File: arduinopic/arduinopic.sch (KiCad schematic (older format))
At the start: 19 parts, among them Q1 BC847, U1 PIC16F628-xxIP, U2 PIC16F610-IP

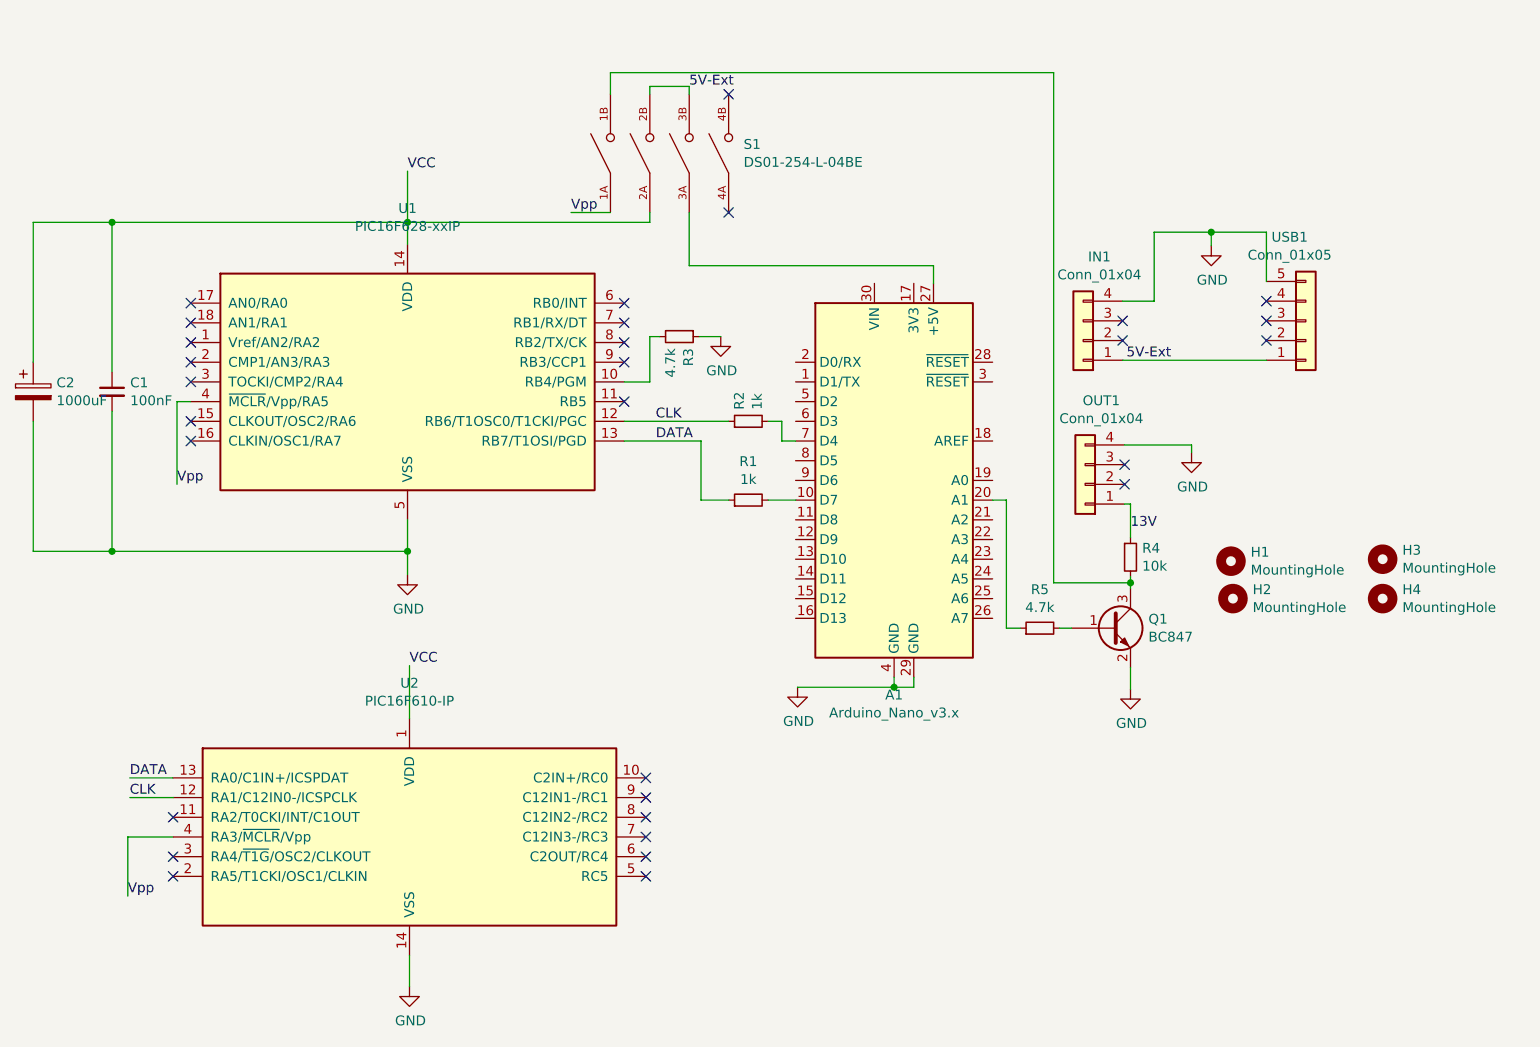
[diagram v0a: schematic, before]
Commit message: PIC12F629, PIC12F675 support added
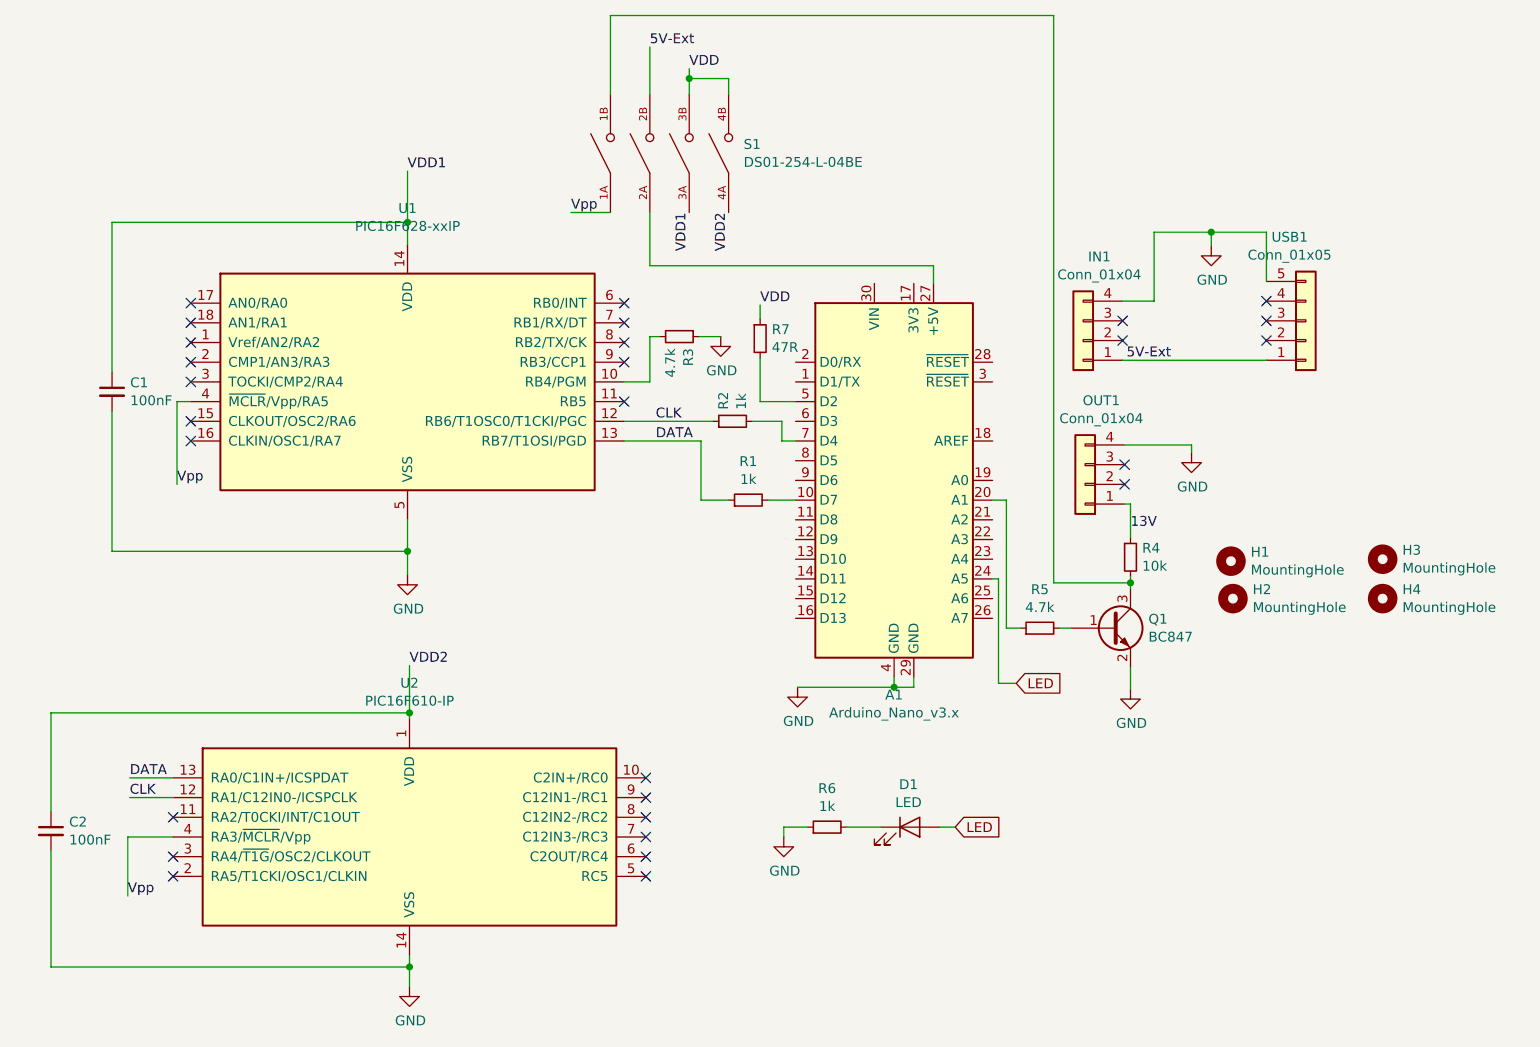
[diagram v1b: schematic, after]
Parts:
- removed C2: 1000uF, Capacitor_THT:CP_Radial_D10.0mm_P5.00mm, symbol Device:CP
- added C2: 100nF, Capacitor_SMD:C_1206_3216Metric_Pad1.42x1.75mm_HandSolder, symbol Device:C_Small
- added D1: LED, LED_SMD:LED_1206_3216Metric_Pad1.42x1.75mm_HandSolder, symbol Device:LED
- added R6: 1k, Resistor_SMD:R_1206_3216Metric_Pad1.42x1.75mm_HandSolder, symbol Device:R_Small
- added R7: 47R, Resistor_SMD:R_1206_3216Metric_Pad1.42x1.75mm_HandSolder, symbol Device:R_Small
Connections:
- net 5V-Ext: no longer S1.3B
- net GND: now also C2.2, R6.1
- net LED: now reaches A1.24 (A5)
- net LED: now also D1.2 (A)
- net at A1.27 (+5V): now also S1.2A; no longer S1.3A
- net at A1.5 (D2): now also R7.2
- net VDD2: now reaches S1.4A
- net VDD2: now also U2.1 (VDD), C2.1
- net VDD: now reaches S1.4B
- net VDD: now also S1.3B, R7.1
- net VCC renamed VDD1
- net VDD1: now also S1.3A; no longer S1.2A, U2.1 (VDD)
- new net: D1.1 (K), R6.2
- no-connect marks 30 -> 28
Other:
- moved on the sheet: R2
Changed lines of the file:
@@
 L Device:R_Small R2
 U 1 1 6091C76F
-P 4820 3100
-F 0 "R2" H 4879 3146 50  0000 L CNN
-F 1 "1k" H 4879 3055 50  0000 L CNN
-F 2 "Resistor_SMD:R_1206_3216Metric_Pad1.42x1.75mm_HandSolder" H 4820 3100 50  0001 C CNN
-F 3 "~" H 4820 3100 50  0001 C CNN
-	1    4820 3100
+P 4740 3100
+F 0 "R2" H 4799 3146 50  0000 L CNN
+F 1 "1k" H 4799 3055 50  0000 L CNN
+F 2 "Resistor_SMD:R_1206_3216Metric_Pad1.42x1.75mm_HandSolder" H 4740 3100 50  0001 C CNN
+F 3 "~" H 4740 3100 50  0001 C CNN
+	1    4740 3100
 	0    -1   -1   0
 $EndComp
@@
 Wire Wire Line
 	5560 4450 5660 4450
-Text Label 4520 1410 0    50   ~ 0
+Text Label 4320 1200 0    50   ~ 0
 5V-Ext
 $Comp
@@
 	4190 2900 4320 2900
 Wire Wire Line
-	1190 2800 1190 2090
-Wire Wire Line
-	1190 2090 1590 2090
-Connection ~ 1590 2090
-Wire Wire Line
-	1190 3100 1190 3760
-Wire Wire Line
-	1190 3760 1590 3760
-Connection ~ 1590 3760
-$Comp
-L Device:CP C2
-U 1 1 609E451B
-P 1190 2950
-F 0 "C2" H 1308 2996 50  0000 L CNN
-F 1 "1000uF" H 1308 2905 50  0000 L CNN
-F 2 "Capacitor_THT:CP_Radial_D10.0mm_P5.00mm" H 1228 2800 50  0001 C CNN
-F 3 "~" H 1190 2950 50  0001 C CNN
-	1    1190 2950
-	1    0    0    -1
-$EndComp
-Wire Wire Line
 	7070 3260 7070 3220
 Wire Wire Line
@@
 Wire Wire Line
 	7170 2140 7450 2140
-$Comp
-L DS01-254-L-04BE:DS01-254-L-04BE S1
-U 1 1 609FF835
-P 4420 1740
-F 0 "S1" V 4466 1364 50  0000 R CNN
-F 1 "DS01-254-L-04BE" V 4375 1364 50  0000 R CNN
-F 2 "SW_DS01-254-L-04BE" H 4420 1740 50  0001 L BNN
-F 3 "" H 4420 1740 50  0001 L BNN
-F 4 "CUI" H 4420 1740 50  0001 L BNN "MANUFACTURER"
-F 5 "1.0" H 4420 1740 50  0001 L BNN "PARTREV"
-F 6 "7.0mm" H 4420 1740 50  0001 L BNN "MAXIMUM_PACKAGE_HEIGHT"
-F 7 "Manufacturer recommendations" H 4420 1740 50  0001 L BNN "STANDARD"
-	1    4420 1740
-	0    -1   -1   0
-$EndComp
 Wire Wire Line
 	3090 2200 3090 2090
@@
 Wire Wire Line
 	5760 2310 5760 2400
-Wire Wire Line
-	6370 3920 6370 1330
 Wire Wire Line
 	6370 3920 6760 3920
@@
 $EndComp
 Wire Wire Line
-	4190 3100 4720 3100
-Wire Wire Line
-	4920 3100 4990 3100
+	4190 3100 4640 3100
+Wire Wire Line
+	4840 3100 4990 3100
 Wire Wire Line
 	4990 3100 4990 3200
@@
 $EndComp
 Wire Wire Line
-	3100 5970 3100 5810
-Text Label 3090 1830 0    50   ~ 0
-VCC
+	3100 5970 3100 5870
 Wire Wire Line
 	3090 2090 3090 1830
-Text Label 3100 4340 0    50   ~ 0
-VCC
-Wire Wire Line
-	3100 4610 3100 4340
+Wire Wire Line
+	3100 4610 3100 4580
 Wire Wire Line
 	4920 3500 5060 3500
@@
 Wire Wire Line
 	1680 5010 1900 5010
-Wire Wire Line
-	4520 2040 4520 2310
-Wire Wire Line
-	4520 2310 5760 2310
-Wire Wire Line
-	4320 2090 4320 2040
-Wire Wire Line
-	3090 2090 4320 2090
-Wire Wire Line
-	4120 1330 6370 1330
-Wire Wire Line
-	4120 1330 4120 1440
-Wire Wire Line
-	4320 1440 4320 1400
-Wire Wire Line
-	4320 1400 4520 1400
-Wire Wire Line
-	4520 1400 4520 1440
 Text Label 3920 2040 0    50   ~ 0
 Vpp
 Wire Wire Line
 	4120 2040 3920 2040
-NoConn ~ 4720 1440
-NoConn ~ 4720 2040
 NoConn ~ 1990 2500
 NoConn ~ 1990 2600
@@
 NoConn ~ 6730 3320
 NoConn ~ 6730 3420
+$Comp
+L Device:LED D1
+U 1 1 6166A7FB
+P 5640 5160
+F 0 "D1" H 5633 5376 50  0000 C CNN
+F 1 "LED" H 5633 5285 50  0000 C CNN
+F 2 "LED_SMD:LED_1206_3216Metric_Pad1.42x1.75mm_HandSolder" H 5640 5160 50  0001 C CNN
+F 3 "~" H 5640 5160 50  0001 C CNN
+	1    5640 5160
+	1    0    0    -1
+$EndComp
+$Comp
+L Device:R_Small R6
+U 1 1 6166BA64
+P 5220 5160
+F 0 "R6" V 5416 5160 50  0000 C CNN
+F 1 "1k" V 5325 5160 50  0000 C CNN
+F 2 "Resistor_SMD:R_1206_3216Metric_Pad1.42x1.75mm_HandSolder" H 5220 5160 50  0001 C CNN
+F 3 "~" H 5220 5160 50  0001 C CNN
+	1    5220 5160
+	0    -1   -1   0
+$EndComp
+Wire Wire Line
+	5320 5160 5490 5160
+Wire Wire Line
+	5120 5160 5000 5160
+Wire Wire Line
+	5000 5160 5000 5210
+$Comp
+L power:GND #PWR0108
+U 1 1 61670669
+P 5000 5210
+F 0 "#PWR0108" H 5000 4960 50  0001 C CNN
+F 1 "GND" H 5005 5037 50  0000 C CNN
+F 2 "" H 5000 5210 50  0001 C CNN
+F 3 "" H 5000 5210 50  0001 C CNN
+	1    5000 5210
+	1    0    0    -1
+$EndComp
+Text GLabel 6180 4430 2    50   Input ~ 0
+LED
+Wire Wire Line
+	6060 3900 6090 3900
+Wire Wire Line
+	6090 4430 6180 4430
+Wire Wire Line
+	6090 3900 6090 4430
+Text GLabel 5870 5160 2    50   Input ~ 0
+LED
+Wire Wire Line
+	5790 5160 5870 5160
+Text Label 4880 2510 0    50   ~ 0
+VDD
+Wire Wire Line
+	4880 3000 5060 3000
+Wire Wire Line
+	4880 2780 4880 3000
+$Comp
+L Device:R_Small R7
+U 1 1 6168982C
+P 4880 2680
+F 0 "R7" H 4939 2726 50  0000 L CNN
+F 1 "47R" H 4939 2635 50  0000 L CNN
+F 2 "Resistor_SMD:R_1206_3216Metric_Pad1.42x1.75mm_HandSolder" H 4880 2680 50  0001 C CNN
+F 3 "~" H 4880 2680 50  0001 C CNN
+	1    4880 2680
+	1    0    0    -1
+$EndComp
+Wire Wire Line
+	4880 2580 4880 2510
+Text Label 3090 1830 0    50   ~ 0
+VDD1
+Text Label 3100 4340 0    50   ~ 0
+VDD2
+Wire Wire Line
+	4320 2040 4320 2310
+Wire Wire Line
+	4320 2310 5760 2310
+Text Label 4520 1310 0    50   ~ 0
+VDD
+Wire Wire Line
+	4320 1200 4320 1440
+Wire Wire Line
+	4120 1040 6370 1040
+Wire Wire Line
+	4120 1040 4120 1440
+Wire Wire Line
+	6370 1040 6370 3920
+Wire Wire Line
+	4520 1440 4520 1360
+Wire Wire Line
+	4520 1360 4720 1360
+Connection ~ 4520 1360
+Wire Wire Line
+	4520 1360 4520 1310
+Wire Wire Line
+	4720 1360 4720 1440
+$Comp
+L DS01-254-L-04BE:DS01-254-L-04BE S1
+U 1 1 609FF835
+P 4420 1740
+F 0 "S1" V 4466 1364 50  0000 R CNN
+F 1 "DS01-254-L-04BE" V 4375 1364 50  0000 R CNN
+F 2 "SW_DS01-254-L-04BE" H 4420 1740 50  0001 L BNN
+F 3 "" H 4420 1740 50  0001 L BNN
+F 4 "CUI" H 4420 1740 50  0001 L BNN "MANUFACTURER"
+F 5 "1.0" H 4420 1740 50  0001 L BNN "PARTREV"
+F 6 "7.0mm" H 4420 1740 50  0001 L BNN "MAXIMUM_PACKAGE_HEIGHT"
+F 7 "Manufacturer recommendations" H 4420 1740 50  0001 L BNN "STANDARD"
+	1    4420 1740
+	0    -1   -1   0
+$EndComp
+Text Label 4520 2040 3    50   ~ 0
+VDD1
+Text Label 4720 2040 3    50   ~ 0
+VDD2
+$Comp
+L Device:C_Small C2
+U 1 1 6169EEC3
+P 1280 5180
+F 0 "C2" H 1372 5226 50  0000 L CNN
+F 1 "100nF" H 1372 5135 50  0000 L CNN
+F 2 "Capacitor_SMD:C_1206_3216Metric_Pad1.42x1.75mm_HandSolder" H 1280 5180 50  0001 C CNN
+F 3 "~" H 1280 5180 50  0001 C CNN
+	1    1280 5180
+	1    0    0    -1
+$EndComp
+Wire Wire Line
+	1280 5080 1280 4580
+Wire Wire Line
+	1280 4580 3100 4580
+Connection ~ 3100 4580
+Wire Wire Line
+	3100 4580 3100 4340
+Wire Wire Line
+	1280 5280 1280 5870
+Wire Wire Line
+	1280 5870 3100 5870
+Connection ~ 3100 5870
+Wire Wire Line
+	3100 5870 3100 5810
 $EndSCHEMATC
